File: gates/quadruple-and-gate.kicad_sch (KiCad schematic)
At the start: 0 parts

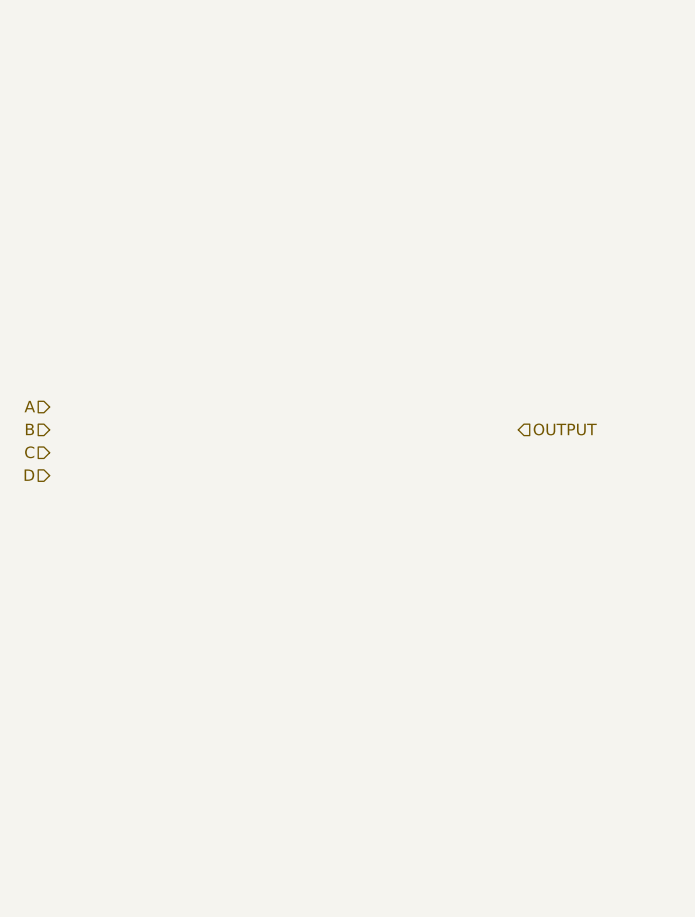
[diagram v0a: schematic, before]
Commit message: Alternative and gates with different amounts of inputs
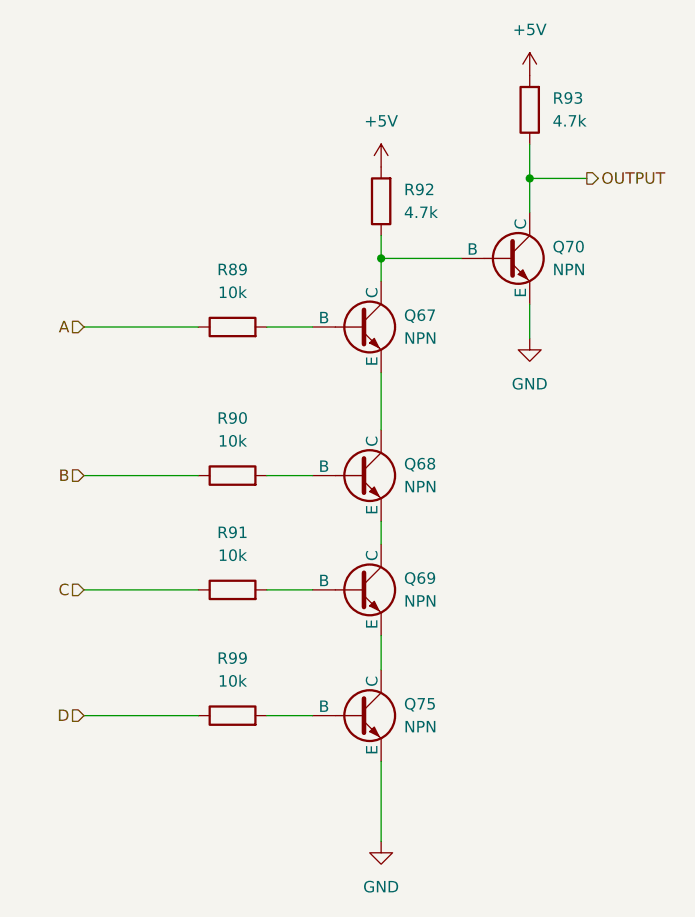
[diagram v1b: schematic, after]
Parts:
- added Q67, Q68, Q69, Q70, Q75: NPN, SOT-23-3_L2.9-W1.6-P1.90-LS2.8-BR:SOT-23-3_L2.9-W1.6-P1.90-LS2.8-BR, symbol Simulation_SPICE:NPN
- added R89, R90, R91, R99: 10k, R0603:R0603, symbol Device:R
- added R92, R93: 4.7k, R0603:R0603, symbol Device:R
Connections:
- net A: now also R89.1
- net B: now also R90.1
- net C: now also R91.1
- net D: now also R99.1
- net OUTPUT: now also Q70.1 (C), R93.1
- new net: Q75.2 (B), R99.2
- new net: Q67.2 (B), R89.2
- new net: Q67.3 (E), Q68.1 (C)
- new net: Q68.2 (B), R90.2
- new net: Q68.3 (E), Q69.1 (C)
- new net: Q67.1 (C), Q70.2 (B), R92.1
- new net: Q69.2 (B), R91.2
- new net: Q69.3 (E), Q75.1 (C)
- new net +5V: R92.2, R93.2
- new net GND: Q70.3 (E), Q75.3 (E)

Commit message: complete 2-bit encoder
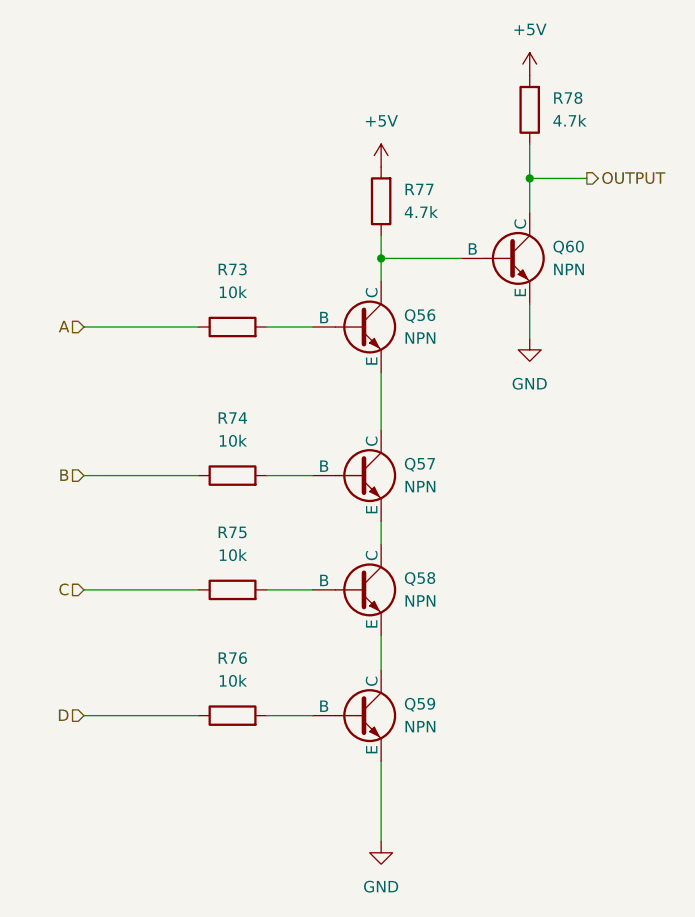
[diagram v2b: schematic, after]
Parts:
- renumbered Q67 to Q56, Q68 to Q57, Q69 to Q58, Q75 to Q59, Q70 to Q60, R89 to R73, R90 to R74, R91 to R75, R99 to R76, R92 to R77, R93 to R78
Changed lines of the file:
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@@
 		(dnp no)
 		(fields_autoplaced yes)
-		(property "Reference" "R99"
+		(property "Reference" "R76"
 			(at 121.92 101.6 90)
 			(effects
@@
 			(project "control-unit"
 				(path "/1cf3a7ee-ec47-45b6-b515-1840d726ab8f/26359086-ff71-45be-b2f3-6346ead43f2c"
-					(reference "R99")
+					(reference "R76")
 					(unit 1)
 				)
 				(path "/1cf3a7ee-ec47-45b6-b515-1840d726ab8f/862b373d-048f-49c8-8545-52f35fa09436"
-					(reference "R100")
+					(reference "R95")
 					(unit 1)
 				)
@@
 		(dnp no)
 		(fields_autoplaced yes)
-		(property "Reference" "R89"
+		(property "Reference" "R73"
 			(at 121.92 58.42 90)
 			(effects
@@
 			(project "control-unit"
 				(path "/1cf3a7ee-ec47-45b6-b515-1840d726ab8f/26359086-ff71-45be-b2f3-6346ead43f2c"
-					(reference "R89")
+					(reference "R73")
 					(unit 1)
 				)
 				(path "/1cf3a7ee-ec47-45b6-b515-1840d726ab8f/862b373d-048f-49c8-8545-52f35fa09436"
-					(reference "R94")
+					(reference "R92")
 					(unit 1)
 				)
@@
 		(dnp no)
 		(fields_autoplaced yes)
-		(property "Reference" "Q68"
+		(property "Reference" "Q57"
 			(at 140.97 80.0099 0)
 			(effects
@@
 			(project "control-unit"
 				(path "/1cf3a7ee-ec47-45b6-b515-1840d726ab8f/26359086-ff71-45be-b2f3-6346ead43f2c"
-					(reference "Q68")
+					(reference "Q57")
 					(unit 1)
 				)
@@
 		(dnp no)
 		(fields_autoplaced yes)
-		(property "Reference" "#PWR081"
+		(property "Reference" "#PWR068"
 			(at 138.43 50.8 0)
 			(effects
@@
 			)
 		)
-		(property "Description" ""
+		(property "Description" "Power symbol creates a global label with name \"+5V\""
 			(at 138.43 46.99 0)
 			(effects
@@
 			(project "control-unit"
 				(path "/1cf3a7ee-ec47-45b6-b515-1840d726ab8f/26359086-ff71-45be-b2f3-6346ead43f2c"
-					(reference "#PWR081")
+					(reference "#PWR068")
 					(unit 1)
 				)
 				(path "/1cf3a7ee-ec47-45b6-b515-1840d726ab8f/862b373d-048f-49c8-8545-52f35fa09436"
-					(reference "#PWR085")
+					(reference "#PWR084")
 					(unit 1)
 				)
@@
 		(dnp no)
 		(fields_autoplaced yes)
-		(property "Reference" "Q67"
+		(property "Reference" "Q56"
 			(at 140.97 63.4999 0)
 			(effects
@@
 			(project "control-unit"
 				(path "/1cf3a7ee-ec47-45b6-b515-1840d726ab8f/26359086-ff71-45be-b2f3-6346ead43f2c"
-					(reference "Q67")
+					(reference "Q56")
 					(unit 1)
 				)
@@
 		(dnp no)
 		(fields_autoplaced yes)
-		(property "Reference" "R93"
+		(property "Reference" "R78"
 			(at 157.48 39.3699 0)
 			(effects
@@
 			(project "control-unit"
 				(path "/1cf3a7ee-ec47-45b6-b515-1840d726ab8f/26359086-ff71-45be-b2f3-6346ead43f2c"
-					(reference "R93")
+					(reference "R78")
 					(unit 1)
 				)
 				(path "/1cf3a7ee-ec47-45b6-b515-1840d726ab8f/862b373d-048f-49c8-8545-52f35fa09436"
-					(reference "R98")
+					(reference "R97")
 					(unit 1)
 				)
@@
 		(dnp no)
 		(fields_autoplaced yes)
-		(property "Reference" "Q69"
+		(property "Reference" "Q58"
 			(at 140.97 92.7099 0)
 			(effects
@@
 			(project "control-unit"
 				(path "/1cf3a7ee-ec47-45b6-b515-1840d726ab8f/26359086-ff71-45be-b2f3-6346ead43f2c"
-					(reference "Q69")
+					(reference "Q58")
 					(unit 1)
 				)
@@
 		(dnp no)
 		(fields_autoplaced yes)
-		(property "Reference" "R90"
+		(property "Reference" "R74"
 			(at 121.92 74.93 90)
 			(effects
@@
 			(project "control-unit"
 				(path "/1cf3a7ee-ec47-45b6-b515-1840d726ab8f/26359086-ff71-45be-b2f3-6346ead43f2c"
-					(reference "R90")
+					(reference "R74")
 					(unit 1)
 				)
 				(path "/1cf3a7ee-ec47-45b6-b515-1840d726ab8f/862b373d-048f-49c8-8545-52f35fa09436"
-					(reference "R95")
+					(reference "R93")
 					(unit 1)
 				)
@@
 		(dnp no)
 		(fields_autoplaced yes)
-		(property "Reference" "Q70"
+		(property "Reference" "Q60"
 			(at 157.48 55.8799 0)
 			(effects
@@
 			(project "control-unit"
 				(path "/1cf3a7ee-ec47-45b6-b515-1840d726ab8f/26359086-ff71-45be-b2f3-6346ead43f2c"
-					(reference "Q70")
+					(reference "Q60")
 					(unit 1)
 				)
 				(path "/1cf3a7ee-ec47-45b6-b515-1840d726ab8f/862b373d-048f-49c8-8545-52f35fa09436"
-					(reference "Q74")
+					(reference "Q75")
 					(unit 1)
 				)
@@
 		(dnp no)
 		(fields_autoplaced yes)
-		(property "Reference" "R91"
+		(property "Reference" "R75"
 			(at 121.92 87.63 90)
 			(effects
@@
 			(project "control-unit"
 				(path "/1cf3a7ee-ec47-45b6-b515-1840d726ab8f/26359086-ff71-45be-b2f3-6346ead43f2c"
-					(reference "R91")
+					(reference "R75")
 					(unit 1)
 				)
 				(path "/1cf3a7ee-ec47-45b6-b515-1840d726ab8f/862b373d-048f-49c8-8545-52f35fa09436"
-					(reference "R96")
+					(reference "R94")
 					(unit 1)
 				)
@@
 		(dnp no)
 		(fields_autoplaced yes)
-		(property "Reference" "Q75"
+		(property "Reference" "Q59"
 			(at 140.97 106.6799 0)
 			(effects
@@
 			(project "control-unit"
 				(path "/1cf3a7ee-ec47-45b6-b515-1840d726ab8f/26359086-ff71-45be-b2f3-6346ead43f2c"
-					(reference "Q75")
+					(reference "Q59")
 					(unit 1)
 				)
 				(path "/1cf3a7ee-ec47-45b6-b515-1840d726ab8f/862b373d-048f-49c8-8545-52f35fa09436"
-					(reference "Q76")
+					(reference "Q74")
 					(unit 1)
 				)
@@
 		(dnp no)
 		(fields_autoplaced yes)
-		(property "Reference" "R92"
+		(property "Reference" "R77"
 			(at 140.97 49.5299 0)
 			(effects
@@
 			(project "control-unit"
 				(path "/1cf3a7ee-ec47-45b6-b515-1840d726ab8f/26359086-ff71-45be-b2f3-6346ead43f2c"
-					(reference "R92")
+					(reference "R77")
 					(unit 1)
 				)
 				(path "/1cf3a7ee-ec47-45b6-b515-1840d726ab8f/862b373d-048f-49c8-8545-52f35fa09436"
-					(reference "R97")
+					(reference "R96")
 					(unit 1)
 				)
@@
 		(dnp no)
 		(fields_autoplaced yes)
-		(property "Reference" "#PWR083"
+		(property "Reference" "#PWR070"
 			(at 154.94 40.64 0)
 			(effects
@@
 			)
 		)
-		(property "Description" ""
+		(property "Description" "Power symbol creates a global label with name \"+5V\""
 			(at 154.94 36.83 0)
 			(effects
@@
 			(project "control-unit"
 				(path "/1cf3a7ee-ec47-45b6-b515-1840d726ab8f/26359086-ff71-45be-b2f3-6346ead43f2c"
-					(reference "#PWR083")
+					(reference "#PWR070")
 					(unit 1)
 				)
 				(path "/1cf3a7ee-ec47-45b6-b515-1840d726ab8f/862b373d-048f-49c8-8545-52f35fa09436"
-					(reference "#PWR087")
+					(reference "#PWR086")
 					(unit 1)
 				)
@@
 		(dnp no)
 		(fields_autoplaced yes)
-		(property "Reference" "#PWR082"
+		(property "Reference" "#PWR069"
 			(at 138.43 128.27 0)
 			(effects
@@
 			)
 		)
-		(property "Description" ""
+		(property "Description" "Power symbol creates a global label with name \"GND\" , ground"
 			(at 138.43 121.92 0)
 			(effects
@@
 			(project "control-unit"
 				(path "/1cf3a7ee-ec47-45b6-b515-1840d726ab8f/26359086-ff71-45be-b2f3-6346ead43f2c"
-					(reference "#PWR082")
+					(reference "#PWR069")
 					(unit 1)
 				)
 				(path "/1cf3a7ee-ec47-45b6-b515-1840d726ab8f/862b373d-048f-49c8-8545-52f35fa09436"
-					(reference "#PWR086")
+					(reference "#PWR085")
 					(unit 1)
 				)
@@
 		(dnp no)
 		(fields_autoplaced yes)
-		(property "Reference" "#PWR084"
+		(property "Reference" "#PWR071"
 			(at 154.94 72.39 0)
 			(effects
@@
 			)
 		)
-		(property "Description" ""
+		(property "Description" "Power symbol creates a global label with name \"GND\" , ground"
 			(at 154.94 66.04 0)
 			(effects
@@
 			(project "control-unit"
 				(path "/1cf3a7ee-ec47-45b6-b515-1840d726ab8f/26359086-ff71-45be-b2f3-6346ead43f2c"
-					(reference "#PWR084")
+					(reference "#PWR071")
 					(unit 1)
 				)
 				(path "/1cf3a7ee-ec47-45b6-b515-1840d726ab8f/862b373d-048f-49c8-8545-52f35fa09436"
-					(reference "#PWR088")
-					(unit 1)
-				)
+					(reference "#PWR087")
+					(unit 1)
+				)

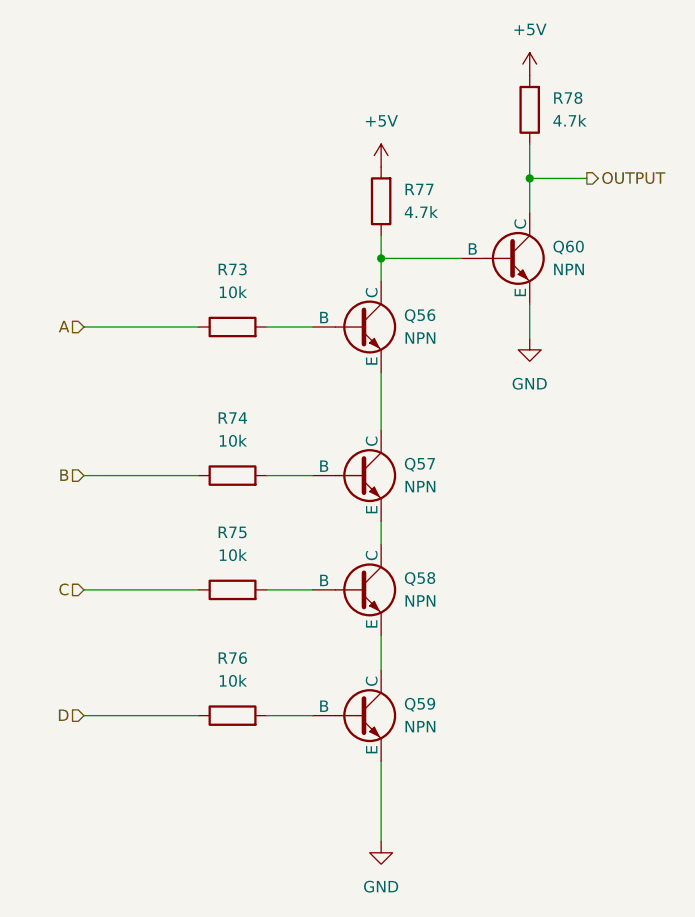
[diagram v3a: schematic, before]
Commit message: Moved wires to more easily do operating point analysis
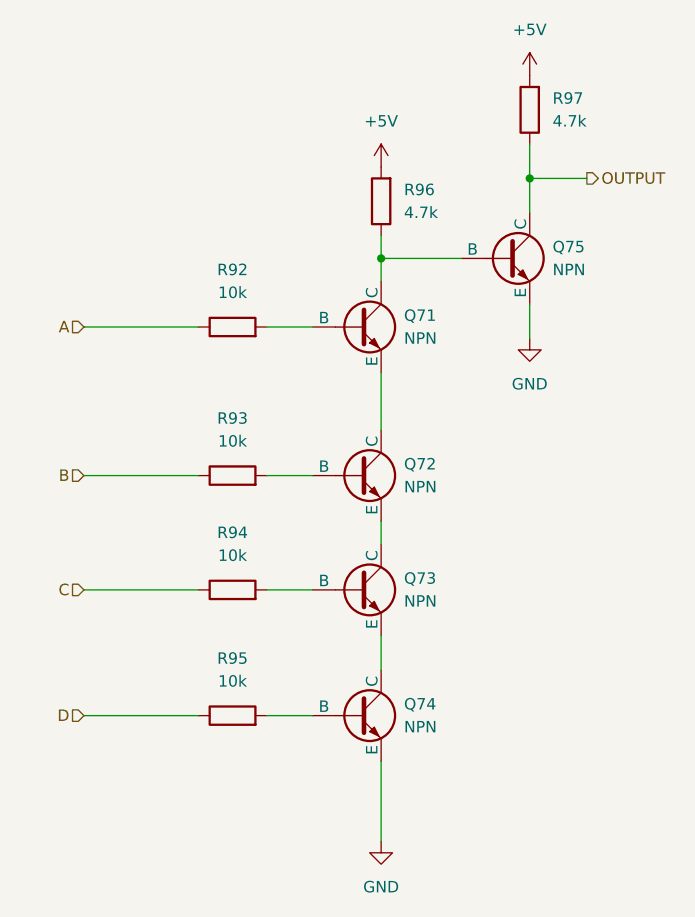
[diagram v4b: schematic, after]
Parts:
- renumbered Q56 to Q71, Q57 to Q72, Q58 to Q73, Q59 to Q74, Q60 to Q75, R73 to R92, R74 to R93, R75 to R94, R76 to R95, R77 to R96, R78 to R97
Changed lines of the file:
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@@
 		(dnp no)
 		(fields_autoplaced yes)
-		(property "Reference" "R76"
+		(property "Reference" "R95"
 			(at 121.92 101.6 90)
 			(effects
@@
 		(dnp no)
 		(fields_autoplaced yes)
-		(property "Reference" "R73"
+		(property "Reference" "R92"
 			(at 121.92 58.42 90)
 			(effects
@@
 		(dnp no)
 		(fields_autoplaced yes)
-		(property "Reference" "Q57"
+		(property "Reference" "Q72"
 			(at 140.97 80.0099 0)
 			(effects
@@
 		(dnp no)
 		(fields_autoplaced yes)
-		(property "Reference" "#PWR068"
+		(property "Reference" "#PWR084"
 			(at 138.43 50.8 0)
 			(effects
@@
 		(dnp no)
 		(fields_autoplaced yes)
-		(property "Reference" "Q56"
+		(property "Reference" "Q71"
 			(at 140.97 63.4999 0)
 			(effects
@@
 		(dnp no)
 		(fields_autoplaced yes)
-		(property "Reference" "R78"
+		(property "Reference" "R97"
 			(at 157.48 39.3699 0)
 			(effects
@@
 		(dnp no)
 		(fields_autoplaced yes)
-		(property "Reference" "Q58"
+		(property "Reference" "Q73"
 			(at 140.97 92.7099 0)
 			(effects
@@
 		(dnp no)
 		(fields_autoplaced yes)
-		(property "Reference" "R74"
+		(property "Reference" "R93"
 			(at 121.92 74.93 90)
 			(effects
@@
 		(dnp no)
 		(fields_autoplaced yes)
-		(property "Reference" "Q60"
+		(property "Reference" "Q75"
 			(at 157.48 55.8799 0)
 			(effects
@@
 		(dnp no)
 		(fields_autoplaced yes)
-		(property "Reference" "R75"
+		(property "Reference" "R94"
 			(at 121.92 87.63 90)
 			(effects
@@
 		(dnp no)
 		(fields_autoplaced yes)
-		(property "Reference" "Q59"
+		(property "Reference" "Q74"
 			(at 140.97 106.6799 0)
 			(effects
@@
 		(dnp no)
 		(fields_autoplaced yes)
-		(property "Reference" "R77"
+		(property "Reference" "R96"
 			(at 140.97 49.5299 0)
 			(effects
@@
 		(dnp no)
 		(fields_autoplaced yes)
-		(property "Reference" "#PWR070"
+		(property "Reference" "#PWR086"
 			(at 154.94 40.64 0)
 			(effects
@@
 		(dnp no)
 		(fields_autoplaced yes)
-		(property "Reference" "#PWR069"
+		(property "Reference" "#PWR085"
 			(at 138.43 128.27 0)
 			(effects
@@
 		(dnp no)
 		(fields_autoplaced yes)
-		(property "Reference" "#PWR071"
+		(property "Reference" "#PWR087"
 			(at 154.94 72.39 0)
 			(effects
